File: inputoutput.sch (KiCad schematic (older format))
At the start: 7 parts, among them J2 UART1, J5 Mini-DIN-6, U1 74HCT04, U11 Z84C30-CTC, U12 Z84C40-SIO-0

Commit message: Added changes to CTC
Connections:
- net labels added: CLK-2
- wire segments 71 -> 72
- no-connect marks 22 -> 21
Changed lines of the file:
@@
 Text Label 5250 3000 2    50   ~ 0
 RxTxCLK
-NoConn ~ 4350 2900
 NoConn ~ 4350 3250
 NoConn ~ 4350 3350
@@
 Wire Wire Line
 	8400 4000 8750 4000
+Text GLabel 4600 2900 2    50   Input ~ 0
+CLK-2
+Wire Wire Line
+	4350 2900 4600 2900
 Wire Bus Line
 	2500 3800 2500 5350

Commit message: Added RTC
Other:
- moved on the sheet: J5, R1, R17, U11, U12, U1D

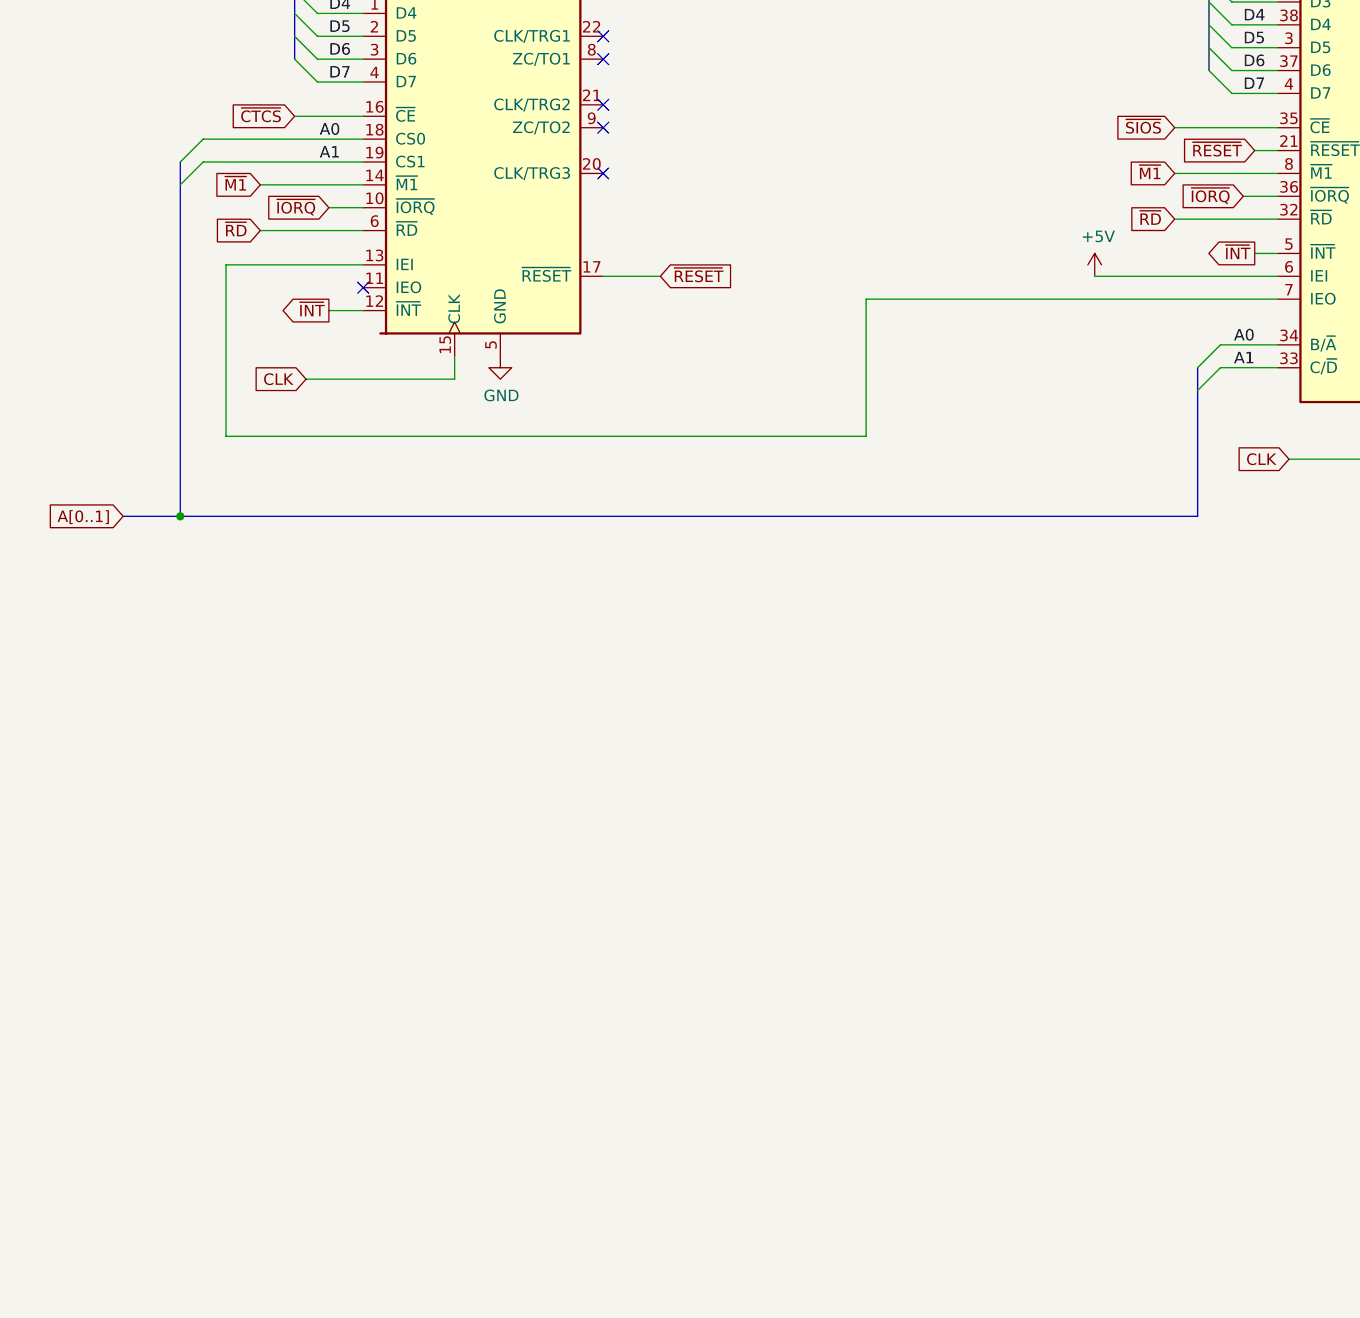
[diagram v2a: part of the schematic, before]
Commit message: Added PIO to schematic
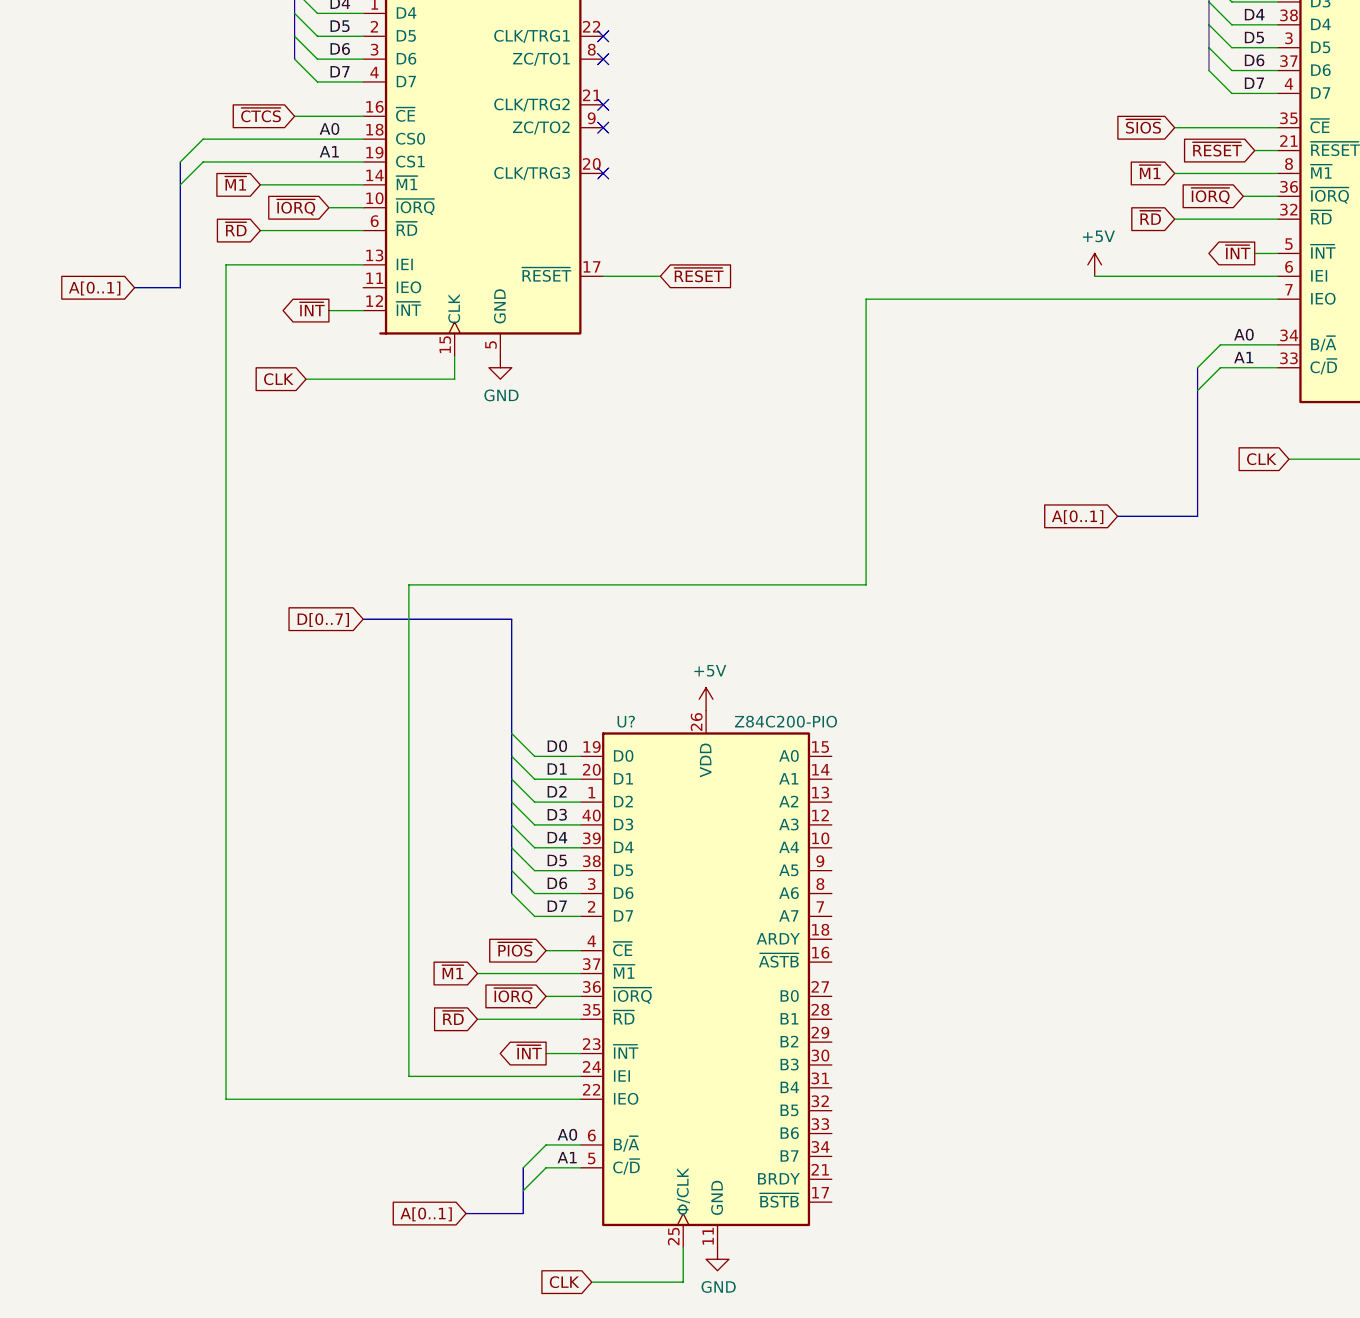
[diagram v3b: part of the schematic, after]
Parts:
- added U?: Z84C200-PIO, Package_DIP:DIP-40_W15.24mm, symbol personal:Z84C200-PIO
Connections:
- net labels added: ~PIOS
- wire segments 72 -> 92
- no-connect marks 21 -> 20
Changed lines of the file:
@@
 NoConn ~ 8050 3550
 NoConn ~ 8050 3650
-NoConn ~ 2950 3250
 $Comp
 L power:+5V #PWR027
@@
 	2650 1050 2000 1050
 Connection ~ 2650 1050
-Text GLabel 1900 4250 0    50   Input ~ 0
+Text GLabel 1950 3250 0    50   Input ~ 0
 A[0..1]
 Wire Wire Line
@@
 	2950 3350 2800 3350
 Wire Bus Line
-	1900 4250 2150 4250
+	1950 3250 2150 3250
 Entry Wire Line
 	6600 3600 6700 3500
@@
 Wire Wire Line
 	6950 3300 5150 3300
-Wire Wire Line
-	5150 3300 5150 3900
-Wire Wire Line
-	5150 3900 2350 3900
-Wire Wire Line
-	2350 3900 2350 3150
-Wire Wire Line
-	2350 3150 2950 3150
 Wire Wire Line
 	8750 1800 8750 1200
@@
 	5700 1200 5700 1900
 Connection ~ 8750 1800
-Connection ~ 2150 4250
-Wire Bus Line
-	2150 4250 6600 4250
 Entry Wire Line
 	2150 2700 2250 2600
@@
 Wire Wire Line
 	4000 1800 4250 1800
-Wire Bus Line
-	2150 2700 2150 4250
+$Comp
+L personal:Z84C200-PIO U?
+U 1 1 6045EEDD
+P 4450 6300
+F 0 "U?" H 4100 7450 50  0000 C CNN
+F 1 "Z84C200-PIO" H 4800 7450 50  0000 C CNN
+F 2 "Package_DIP:DIP-40_W15.24mm" H 4450 6350 50  0001 C CNN
+F 3 "" H 4425 6375 50  0001 C CNN
+	1    4450 6300
+	1    0    0    -1
+$EndComp
+Entry Wire Line
+	3600 5200 3700 5300
+Entry Wire Line
+	3600 5300 3700 5400
+Entry Wire Line
+	3600 5400 3700 5500
+Entry Wire Line
+	3600 5500 3700 5600
+Entry Wire Line
+	3600 5600 3700 5700
+Entry Wire Line
+	3600 5700 3700 5800
+Entry Wire Line
+	3600 5800 3700 5900
+Entry Wire Line
+	3600 5900 3700 6000
+Wire Wire Line
+	3700 5300 3900 5300
+Wire Wire Line
+	3700 5400 3900 5400
+Wire Wire Line
+	3700 5500 3900 5500
+Wire Wire Line
+	3700 5600 3900 5600
+Wire Wire Line
+	3700 5700 3900 5700
+Wire Wire Line
+	3700 5800 3900 5800
+Wire Wire Line
+	3700 5900 3900 5900
+Wire Wire Line
+	3700 6000 3900 6000
+Text Label 3750 5300 0    50   ~ 0
+D0
+Text Label 3750 5400 0    50   ~ 0
+D1
+Text Label 3750 5500 0    50   ~ 0
+D2
+Text Label 3750 5600 0    50   ~ 0
+D3
+Text Label 3750 5700 0    50   ~ 0
+D4
+Text Label 3750 5800 0    50   ~ 0
+D5
+Text Label 3750 5900 0    50   ~ 0
+D6
+Text Label 3750 6000 0    50   ~ 0
+D7
+Text GLabel 2950 4700 0    50   Input ~ 0
+D[0..7]
+Wire Bus Line
+	3600 4700 2950 4700
+Text GLabel 3400 7300 0    50   Input ~ 0
+A[0..1]
+Wire Bus Line
+	3400 7300 3650 7300
+Entry Wire Line
+	3650 7100 3750 7000
+Entry Wire Line
+	3650 7200 3750 7100
+Wire Wire Line
+	3750 7000 3900 7000
+Wire Wire Line
+	3750 7100 3900 7100
+Text Label 3800 7100 0    50   ~ 0
+A1
+Text Label 3800 7000 0    50   ~ 0
+A0
+$Comp
+L power:GND #PWR?
+U 1 1 6047487E
+P 4500 7450
+F 0 "#PWR?" H 4500 7200 50  0001 C CNN
+F 1 "GND" H 4505 7277 50  0000 C CNN
+F 2 "" H 4500 7450 50  0001 C CNN
+F 3 "" H 4500 7450 50  0001 C CNN
+	1    4500 7450
+	1    0    0    -1
+$EndComp
+Text GLabel 3950 7600 0    50   Input ~ 0
+CLK
+Wire Wire Line
+	3950 7600 4350 7600
+Wire Wire Line
+	4350 7600 4350 7450
+$Comp
+L power:+5V #PWR?
+U 1 1 60477A07
+P 4450 5100
+F 0 "#PWR?" H 4450 4950 50  0001 C CNN
+F 1 "+5V" H 4465 5273 50  0000 C CNN
+F 2 "" H 4450 5100 50  0001 C CNN
+F 3 "" H 4450 5100 50  0001 C CNN
+	1    4450 5100
+	1    0    0    -1
+$EndComp
+Text GLabel 3750 6150 0    50   Input ~ 0
+~PIOS
+Wire Wire Line
+	3750 6150 3900 6150
+Text GLabel 3450 6250 0    50   Input ~ 0
+~M1
+Text GLabel 3750 6350 0    50   Input ~ 0
+~IORQ
+Text GLabel 3450 6450 0    50   Input ~ 0
+~RD
+Wire Wire Line
+	3450 6250 3900 6250
+Wire Wire Line
+	3450 6450 3900 6450
+Wire Wire Line
+	3750 6350 3900 6350
+Text GLabel 3750 6600 0    50   Output ~ 0
+~INT
+Wire Wire Line
+	3750 6600 3900 6600
+Wire Wire Line
+	3900 6700 3150 6700
+Wire Wire Line
+	5150 4550 3150 4550
+Wire Wire Line
+	3150 4550 3150 6700
+Wire Wire Line
+	5150 3300 5150 4550
+Wire Wire Line
+	3900 6800 2350 6800
+Wire Wire Line
+	2350 6800 2350 3150
+Wire Wire Line
+	2350 3150 2950 3150
+Text GLabel 6250 4250 0    50   Input ~ 0
+A[0..1]
+Wire Bus Line
+	6250 4250 6600 4250
+Wire Bus Line
+	3650 7100 3650 7300
+Wire Bus Line
+	2150 2700 2150 3250
 Wire Bus Line
 	6600 3600 6600 4250
@@
 Wire Bus Line
 	2650 1050 2650 2250
+Wire Bus Line
+	3600 4700 3600 5900
 $EndSCHEMATC

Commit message: Added circuit for PS/2 host-device communication
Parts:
- removed U1: 74HCT04, symbol 74xx:74HCT04
- added Q? (x3): 2N3904, digikey-footprints:TO-92-3, symbol dk_Transistors-Bipolar-BJT-Single:2N3904
- added R?: 4k7, symbol Device:R
- added U? (x7): 74LS04, symbol 74xx:74LS04
- U?: value Z84C200-PIO -> 74LS04; footprint Package_DIP:DIP-40_W15.24mm -> (none)
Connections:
- wire segments 92 -> 125
- no-connect marks 20 -> 19
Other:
- moved on the sheet: J5, R1, R17, U11, U12, U?

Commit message: Added expansion bus and GPIO ports
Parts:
- removed J2: UART1, symbol Connector_Generic:Conn_01x03
- removed Q?: 2N3904, digikey-footprints:TO-92-3, symbol dk_Transistors-Bipolar-BJT-Single:2N3904
- removed U?: 74LS04, symbol 74xx:74LS04
- added J?: RS232 (TTL Level), symbol Connector:Conn_01x07_Male
- added J?: TimerCounter, symbol Connector:Conn_01x07_Female
- added J?: GPIO1, symbol Connector:Conn_01x12_Female
- added J?: GPIO2, symbol Connector:Conn_01x12_Female
- added R?: 4k7, symbol Device:R
- added U?: 74LS04, symbol 74xx:74LS04
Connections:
- wire segments 125 -> 198
- no-connect marks 19 -> 7
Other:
- note added: "GPIO (Digital IO)"
- note added: "Serial RS232 & PS/2"
- note added: "Timer / Counter"
- moved on the sheet: Q?, R?, U?, U?A, U?B, U?C, U?D, U?F, U?G

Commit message: Updated schematic
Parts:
- added J7: CompactFlash Port, Connector_PinHeader_2.00mm:PinHeader_2x22_P2.00mm_Vertical, symbol Connector_Generic:Conn_02x22_Odd_Even
- J2: renamed from J?; footprint (none) -> Connector_PinSocket_2.54mm:PinSocket_1x07_P2.54mm_Vertical
- J3, J4: renamed from J?; footprint (none) -> Connector_PinSocket_2.54mm:PinSocket_1x12_P2.54mm_Vertical
- J6: renamed from J?; footprint (none) -> Connector_PinHeader_2.54mm:PinHeader_1x07_P2.54mm_Vertical
- R1, R17: footprint (none) -> Resistor_THT:R_Axial_DIN0207_L6.3mm_D2.5mm_P10.16mm_Horizontal
- R13, R14: renamed from R?; footprint (none) -> Resistor_THT:R_Axial_DIN0207_L6.3mm_D2.5mm_P10.16mm_Horizontal
- U11: footprint Package_DIP:DIP-28_W15.24mm -> Package_DIP:DIP-28_W15.24mm_Socket_LongPads
- U12: footprint Package_DIP:DIP-40_W15.24mm -> Package_DIP:DIP-40_W15.24mm_Socket_LongPads
- U14: renamed from U?; value 74LS04 -> Z84C200-PIO; footprint (none) -> Package_DIP:DIP-40_W15.24mm_Socket_LongPads
- U18: renamed from U?; footprint (none) -> Package_DIP:DIP-14_W7.62mm_Socket_LongPads
- gave numbers to parts that had none: 2
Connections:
- net GND: now also U18.13, U18.7 (GND)
- net PA4: now reaches J3.7 (Pin_7), U14.10 (A4)
- net PA3: now reaches J3.6 (Pin_6), U14.12 (A3)
- net PA2: now reaches J3.5 (Pin_5), U14.13 (A2)
- net PA1: now reaches J3.4 (Pin_4), U14.14 (A1)
- net PA0: now reaches J3.3 (Pin_3), U14.15 (A0)
- net ~PASTB: now reaches J3.12 (Pin_12), U14.16 (~ASTB)
- net ~PBSTB: now reaches J4.12 (Pin_12), U14.17 (~BSTB)
- net PARDY: now reaches J3.11 (Pin_11), U14.18 (ARDY)
- net PBRDY: now reaches J4.11 (Pin_11), U14.21 (BRDY)
- net PB0: now reaches J4.3 (Pin_3), U14.27 (B0)
- net PB1: now reaches J4.4 (Pin_4), U14.28 (B1)
- net PB2: now reaches J4.5 (Pin_5), U14.29 (B2)
- net PB3: now reaches J4.6 (Pin_6), U14.30 (B3)
- net PB4: now reaches J4.7 (Pin_7), U14.31 (B4)
- net PB5: now reaches J4.8 (Pin_8), U14.32 (B5)
- net PB6: now reaches J4.9 (Pin_9), U14.33 (B6)
- net PB7: now reaches J4.10 (Pin_10), U14.34 (B7)
- net PA7: now reaches J3.10 (Pin_10), U14.7 (A7)
- net PA6: now reaches J3.9 (Pin_9), U14.8 (A6)
- net PA5: now reaches J3.8 (Pin_8), U14.9 (A5)
- no-connect marks 7 -> 8
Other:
- note added: "Copyright © Jaap Geurts 2021\n\nThis documentation describes Open Hardware and is licensed under the CERN OHL v. 1.1.\nYou may redistribute and modify this documentation under the terms of the CERN OHL v.1.1.\n(http://ohwr.org/cernohl). This documentation is distributed WITHOUT ANY EXPRESS OR IMPLIED\nWARRANTY, INCLUDING OF MERCHANTABILITY, SATISFACTORY QUALITY AND FITNESS FOR A PARTICULAR PURPOS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"

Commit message: All footprints assigned
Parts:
- added D9: CF Activity, LED_THT:LED_D5.0mm, symbol Device:LED
- added JP4: CTS float, Jumper:SolderJumper-2_P1.3mm_Bridged_Pad1.0x1.5mm, symbol Jumper:SolderJumper_2_Bridged
- added R28: 330, Resistor_THT:R_Axial_DIN0207_L6.3mm_D2.5mm_P10.16mm_Horizontal, symbol Device:R
- added R29: 1k, Resistor_THT:R_Axial_DIN0207_L6.3mm_D2.5mm_P10.16mm_Horizontal, symbol Device:R
- J5: footprint (none) -> Personal:Mini_din6
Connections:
- net +5V: now also J7.41 (Pin_41), J7.42 (Pin_42), R28.1, R29.1
- net A0: now also J7.35 (Pin_35)
- net A1: now also J7.33 (Pin_33)
- net D0: now also J7.17 (Pin_17)
- net D1: now also J7.15 (Pin_15)
- net D2: now also J7.13 (Pin_13)
- net D3: now also J7.11 (Pin_11)
- net D4: now also J7.9 (Pin_9)
- net D5: now also J7.7 (Pin_7)
- net D6: now also J7.5 (Pin_5)
- net D7: now also J7.3 (Pin_3)
- net GND: now also J7.19 (Pin_19), JP4.1 (A); no longer U12.23 (~CTSB)
- net ~RD: now also J7.25 (Pin_25)
- net ~RESET: now also J7.1 (Pin_1)
- net at J7.2 (Pin_2): now also J7.22 (Pin_22), J7.24 (Pin_24), J7.26 (Pin_26), J7.30 (Pin_30), J7.40 (Pin_40), J7.43 (Pin_43)
- net ~WR: now reaches J7.23 (Pin_23)
- net A2: now reaches J7.36 (Pin_36)
- net ~CFS: now reaches J7.37 (Pin_37)
- net at J7.38 (Pin_38): now also R29.2
- net at J7.39 (Pin_39): now also D9.1 (K)
- new net: JP4.2 (B), U12.23 (~CTSB)
- new net: D9.2 (A), R28.2
- no-connect marks 8 -> 26
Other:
- note added: "must be half\nclock on pin 15"

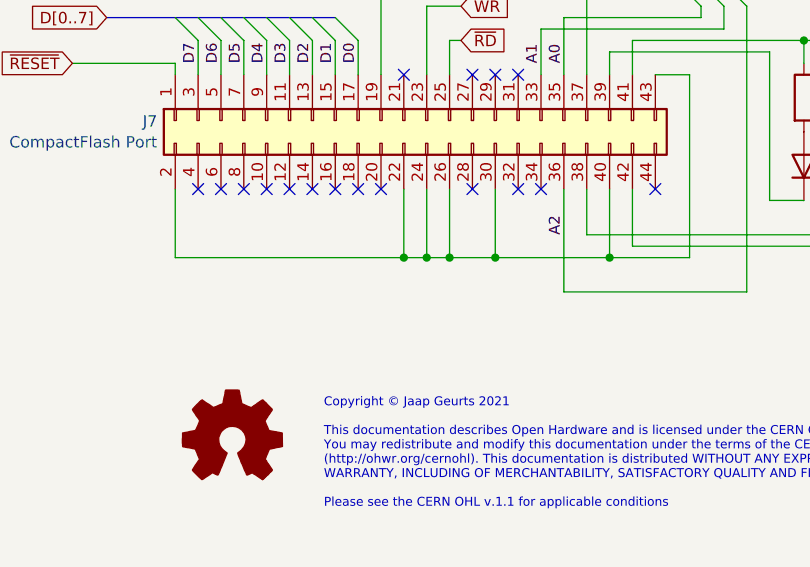
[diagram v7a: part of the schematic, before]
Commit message: PCB tracing done
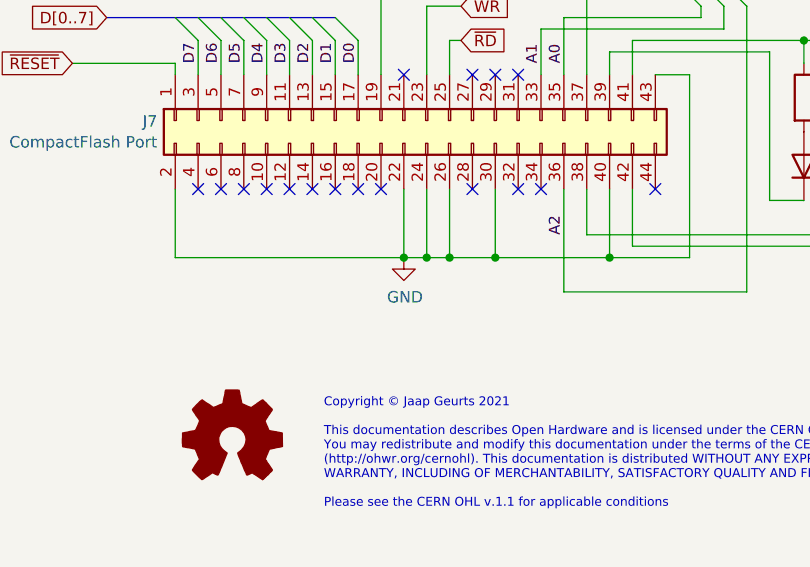
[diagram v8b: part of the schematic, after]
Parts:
- J7: footprint Connector_PinHeader_2.00mm:PinHeader_2x22_P2.00mm_Vertical -> Personal:CompactFlash_Module
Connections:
- net GND: now also J7.2 (Pin_2), J7.22 (Pin_22), J7.24 (Pin_24), J7.26 (Pin_26), J7.30 (Pin_30), J7.40 (Pin_40), J7.43 (Pin_43)
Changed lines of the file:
@@
 F 0 "J7" V 8004 6479 50  0000 L CNN
 F 1 "CompactFlash Port" V 8095 6479 50  0000 L CNN
-F 2 "Connector_PinHeader_2.00mm:PinHeader_2x22_P2.00mm_Vertical" H 8000 5400 50  0001 C CNN
+F 2 "Personal:CompactFlash_Module" H 8000 5400 50  0001 C CNN
 F 3 "~" H 8000 5400 50  0001 C CNN
 	1    8000 5400
@@
 Wire Bus Line
 	1800 1050 1800 2250
+$Comp
+L power:GND #PWR0135
+U 1 1 60E1E285
+P 8000 6000
+F 0 "#PWR0135" H 8000 5750 50  0001 C CNN
+F 1 "GND" H 8005 5827 50  0000 C CNN
+F 2 "" H 8000 6000 50  0001 C CNN
+F 3 "" H 8000 6000 50  0001 C CNN
+	1    8000 6000
+	1    0    0    -1
+$EndComp
 $EndSCHEMATC
